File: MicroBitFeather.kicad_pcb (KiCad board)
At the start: 2 copper layers, 67.3 x 35.6 mm, 16 parts, among them J1 Feather_Long, J2 Barrel_Jack_MountingPin, J3 Feather_Short, J4 NeoPixels, J5 microbit_edge_connector, U1 74AHCT125, U2 MCP1702-3302E_TO92

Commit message: 5V wiring.
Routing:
- net +5V: track 0.00 -> 53.0 mm
- added copper zone on F.Cu, net +5V
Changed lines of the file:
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@@
     (thickness 1.6)
     (drawings 12)
-    (tracks 0)
+    (tracks 16)
     (zones 0)
     (modules 16)
@@
   )
   (setup
-    (last_trace_width 0.25)
+    (last_trace_width 0.508)
+    (user_trace_width 0.508)
+    (user_trace_width 1.016)
     (trace_clearance 0.2)
-    (zone_clearance 0.508)
+    (zone_clearance 0.3048)
     (zone_45_only no)
     (trace_min 0.2)
@@
     (pad_to_mask_clearance 0)
     (aux_axis_origin 0 0)
-    (visible_elements FFFEF77F)
+    (visible_elements FFFEE77F)
     (pcbplotparams
       (layerselection 0x00030_80000001)
@@
   (gr_arc (start 119.38 118.11) (end 119.38 119.38) (angle 90) (layer Edge.Cuts) (width 0.15))
   (gr_arc (start 119.38 85.09) (end 118.11 85.09) (angle 90) (layer Edge.Cuts) (width 0.15))
+  (segment (start 157.48 101.6) (end 154.94 104.14) (width 0.508) (layer F.Cu) (net 1))
+  (segment (start 154.94 104.14) (end 154.94 106.68) (width 0.508) (layer F.Cu) (net 1))
+  (segment (start 133.35 100.33) (end 129.54 96.52) (width 0.508) (layer F.Cu) (net 1))
+  (segment (start 135.89 96.52) (end 135.89 97.79) (width 0.508) (layer F.Cu) (net 1))
+  (segment (start 135.89 97.79) (end 133.35 100.33) (width 0.508) (layer F.Cu) (net 1))
+  (segment (start 140.97 96.52) (end 139.411999 98.078001) (width 1.016) (layer F.Cu) (net 1))
+  (segment (start 139.411999 98.078001) (end 137.448001 98.078001) (width 1.016) (layer F.Cu) (net 1))
+  (segment (start 137.448001 98.078001) (end 135.89 96.52) (width 1.016) (layer F.Cu) (net 1))
+  (segment (start 157.48 101.6) (end 154.94 99.06) (width 1.016) (layer F.Cu) (net 1))
+  (segment (start 154.94 99.06) (end 143.51 99.06) (width 1.016) (layer F.Cu) (net 1))
+  (segment (start 141.819999 97.369999) (end 140.97 96.52) (width 1.016) (layer F.Cu) (net 1))
+  (segment (start 143.51 99.06) (end 141.819999 97.369999) (width 1.016) (layer F.Cu) (net 1))
+  (segment (start 167.005 106.68) (end 164.989 106.68) (width 1.016) (layer F.Cu) (net 1))
+  (segment (start 164.989 106.68) (end 159.909 101.6) (width 1.016) (layer F.Cu) (net 1))
+  (segment (start 159.909 101.6) (end 158.61137 101.6) (width 1.016) (layer F.Cu) (net 1))
+  (segment (start 158.61137 101.6) (end 157.48 101.6) (width 1.016) (layer F.Cu) (net 1))
+  (zone (net 1) (net_name +5V) (layer F.Cu) (hatch edge 0.508)
+    (connect_pads (clearance 0.3048))
+    (min_thickness 0.254)
+    (fill (arc_segments 16) (thermal_gap 0.508) (thermal_bridge_width 0.508))
+    (polygon
+      (pts
+        (xy 180.34 114.3) (xy 166.37 114.3) (xy 166.37 100.33) (xy 180.34 100.33)
+      )
+    )
+  )
 )

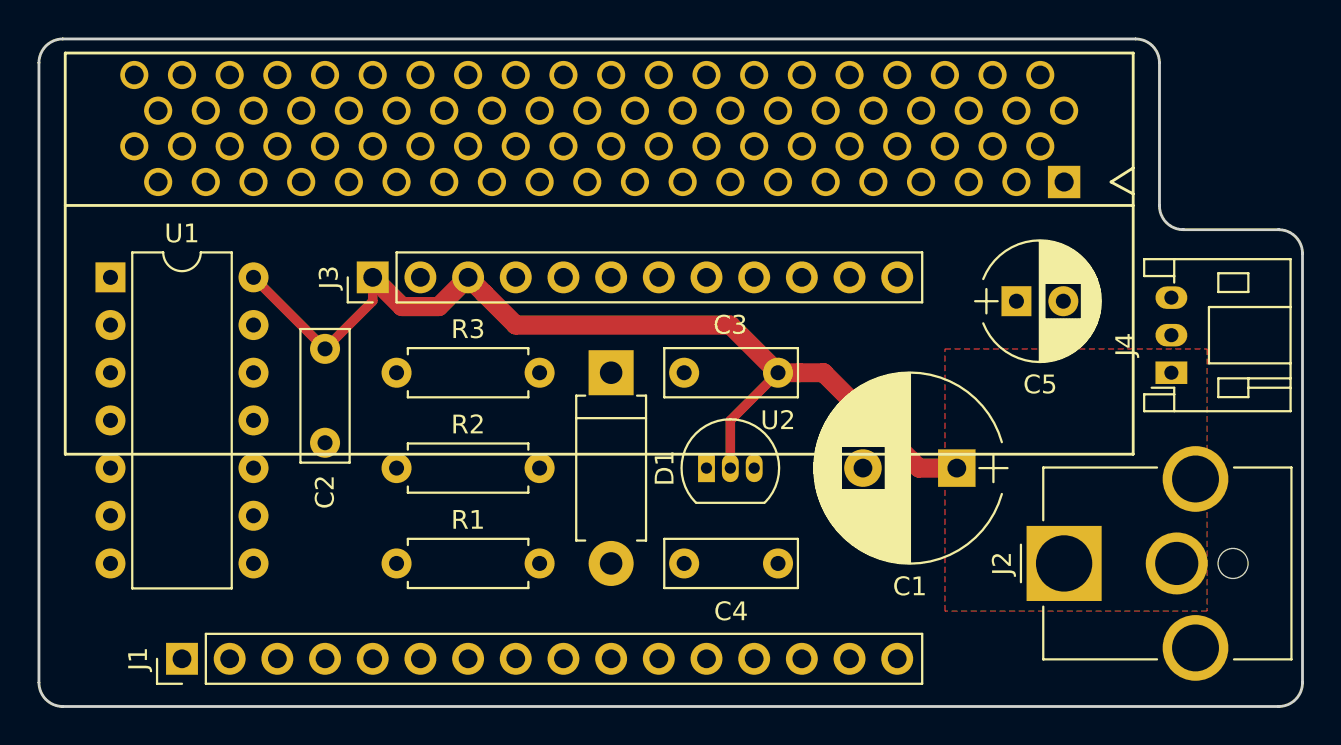
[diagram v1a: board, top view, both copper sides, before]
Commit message: 3V3 wiring.
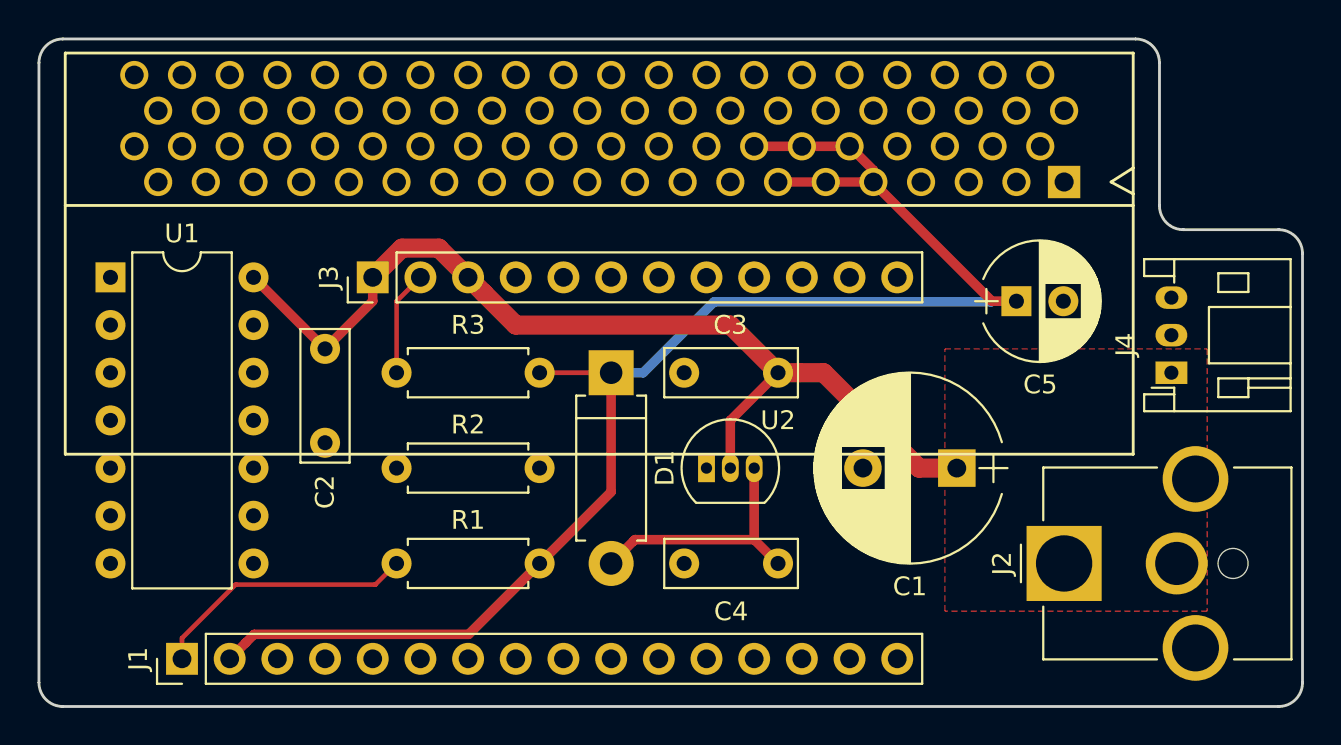
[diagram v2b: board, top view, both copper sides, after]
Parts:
- moved R3 7.62 mm to (144.8, 101.6), turned to 180 degrees
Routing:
- net +3V3: track 0.00 -> 80.2 mm
- net Net-(J1-Pad1): track 0.00 -> 14.2 mm
- net Net-(C4-Pad1): track 0.00 -> 13.8 mm
- net Net-(J3-Pad2): track 0.00 -> 5.61 mm
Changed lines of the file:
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@@
   (general
     (links 79)
-    (no_connects 79)
+    (no_connects 71)
     (area 115.424999 71.584999 217.260002 148.48)
     (thickness 1.6)
     (drawings 12)
-    (tracks 16)
+    (tracks 48)
     (zones 0)
     (modules 16)
@@
   )
   (module Resistors_THT:R_Axial_DIN0207_L6.3mm_D2.5mm_P7.62mm_Horizontal (layer F.Cu)
-    (at 137.16 101.6)
+    (at 144.78 101.6 180)
     (descr "Resistor, Axial_DIN0207 series, Axial, Horizontal, pin pitch=7.62mm, 0.25W = 1/4W, length*diameter=6.3*2.5mm^2, http://cdn-reichelt.de/documents/datenblatt/B400/1_4W%23YAG.pdf")
     (tags "Resistor Axial_DIN0207 series Axial Horizontal pin pitch 7.62mm 0.25W = 1/4W length 6.3mm diameter 2.5mm")
-    (fp_text reference R3 (at 3.81 -2.31) (layer F.SilkS)
-      (effects (font (size 1 1) (thickness 0.15)))
-    )
-    (fp_text value 10K (at 3.81 2.31) (layer F.Fab)
+    (fp_text reference R3 (at 3.81 2.54 180) (layer F.SilkS)
+      (effects (font (size 1 1) (thickness 0.15)))
+    )
+    (fp_text value 10K (at 3.81 2.31 180) (layer F.Fab)
       (effects (font (size 1 1) (thickness 0.15)))
     )
@@
     (fp_line (start 8.7 1.6) (end 8.7 -1.6) (layer F.CrtYd) (width 0.05))
     (fp_line (start 8.7 -1.6) (end -1.05 -1.6) (layer F.CrtYd) (width 0.05))
-    (pad 1 thru_hole circle (at 0 0) (size 1.6 1.6) (drill 0.8) (layers *.Cu *.Mask)
+    (pad 1 thru_hole circle (at 0 0 180) (size 1.6 1.6) (drill 0.8) (layers *.Cu *.Mask)
       (net 4 +3V3))
-    (pad 2 thru_hole oval (at 7.62 0) (size 1.6 1.6) (drill 0.8) (layers *.Cu *.Mask)
+    (pad 2 thru_hole oval (at 7.62 0 180) (size 1.6 1.6) (drill 0.8) (layers *.Cu *.Mask)
       (net 19 "Net-(J3-Pad2)"))
     (model ${KISYS3DMOD}/Resistors_THT.3dshapes/R_Axial_DIN0207_L6.3mm_D2.5mm_P7.62mm_Horizontal.wrl
@@
   (gr_arc (start 119.38 118.11) (end 119.38 119.38) (angle 90) (layer Edge.Cuts) (width 0.15))
   (gr_arc (start 119.38 85.09) (end 118.11 85.09) (angle 90) (layer Edge.Cuts) (width 0.15))
+  (segment (start 140.97 96.52) (end 139.411999 94.961999) (width 1.016) (layer F.Cu) (net 1))
+  (segment (start 139.411999 94.961999) (end 137.448001 94.961999) (width 1.016) (layer F.Cu) (net 1))
+  (segment (start 137.448001 94.961999) (end 135.89 96.52) (width 1.016) (layer F.Cu) (net 1))
   (segment (start 157.48 101.6) (end 154.94 104.14) (width 0.508) (layer F.Cu) (net 1))
   (segment (start 154.94 104.14) (end 154.94 106.68) (width 0.508) (layer F.Cu) (net 1))
@@
   (segment (start 135.89 96.52) (end 135.89 97.79) (width 0.508) (layer F.Cu) (net 1))
   (segment (start 135.89 97.79) (end 133.35 100.33) (width 0.508) (layer F.Cu) (net 1))
-  (segment (start 140.97 96.52) (end 139.411999 98.078001) (width 1.016) (layer F.Cu) (net 1))
-  (segment (start 139.411999 98.078001) (end 137.448001 98.078001) (width 1.016) (layer F.Cu) (net 1))
-  (segment (start 137.448001 98.078001) (end 135.89 96.52) (width 1.016) (layer F.Cu) (net 1))
   (segment (start 157.48 101.6) (end 154.94 99.06) (width 1.016) (layer F.Cu) (net 1))
   (segment (start 154.94 99.06) (end 143.51 99.06) (width 1.016) (layer F.Cu) (net 1))
@@
   (segment (start 159.909 101.6) (end 158.61137 101.6) (width 1.016) (layer F.Cu) (net 1))
   (segment (start 158.61137 101.6) (end 157.48 101.6) (width 1.016) (layer F.Cu) (net 1))
+  (segment (start 156.21 110.49) (end 149.86 110.49) (width 0.508) (layer F.Cu) (net 3))
+  (segment (start 149.86 110.49) (end 149.789999 110.560001) (width 0.508) (layer F.Cu) (net 3))
+  (segment (start 149.789999 110.560001) (end 148.59 111.76) (width 0.508) (layer F.Cu) (net 3))
+  (segment (start 156.21 106.68) (end 156.21 110.49) (width 0.508) (layer F.Cu) (net 3))
+  (segment (start 156.21 110.49) (end 157.48 111.76) (width 0.508) (layer F.Cu) (net 3))
+  (segment (start 158.75 89.54) (end 156.21 89.54) (width 0.508) (layer F.Cu) (net 4))
+  (segment (start 161.29 89.54) (end 158.75 89.54) (width 0.508) (layer F.Cu) (net 4))
+  (segment (start 162.56 91.44) (end 162.56 90.81) (width 0.508) (layer F.Cu) (net 4))
+  (segment (start 162.56 90.81) (end 161.29 89.54) (width 0.508) (layer F.Cu) (net 4))
+  (segment (start 160.02 91.44) (end 157.48 91.44) (width 0.508) (layer F.Cu) (net 4))
+  (segment (start 162.56 91.44) (end 160.02 91.44) (width 0.508) (layer F.Cu) (net 4))
+  (segment (start 170.18 97.79) (end 168.872 97.79) (width 0.508) (layer F.Cu) (net 4))
+  (segment (start 168.872 97.79) (end 162.56 91.478) (width 0.508) (layer F.Cu) (net 4))
+  (segment (start 162.56 91.478) (end 162.56 91.44) (width 0.508) (layer F.Cu) (net 4))
+  (segment (start 144.78 111.76) (end 141.004001 115.535999) (width 0.508) (layer F.Cu) (net 4))
+  (segment (start 141.004001 115.535999) (end 129.574001 115.535999) (width 0.508) (layer F.Cu) (net 4))
+  (segment (start 129.574001 115.535999) (end 129.119999 115.990001) (width 0.508) (layer F.Cu) (net 4))
+  (segment (start 129.119999 115.990001) (end 128.27 116.84) (width 0.508) (layer F.Cu) (net 4))
+  (segment (start 148.59 101.6) (end 148.59 107.95) (width 0.508) (layer F.Cu) (net 4))
+  (segment (start 148.59 107.95) (end 144.78 111.76) (width 0.508) (layer F.Cu) (net 4))
+  (segment (start 148.59 101.6) (end 144.78 101.6) (width 0.25) (layer F.Cu) (net 4))
+  (segment (start 148.59 101.6) (end 150.298 101.6) (width 0.508) (layer B.Cu) (net 4))
+  (segment (start 150.298 101.6) (end 154.073999 97.824001) (width 0.508) (layer B.Cu) (net 4))
+  (segment (start 154.073999 97.824001) (end 168.837999 97.824001) (width 0.508) (layer B.Cu) (net 4))
+  (segment (start 168.837999 97.824001) (end 168.872 97.79) (width 0.508) (layer B.Cu) (net 4))
+  (segment (start 168.872 97.79) (end 170.18 97.79) (width 0.508) (layer B.Cu) (net 4))
+  (segment (start 137.16 111.76) (end 136.034999 112.885001) (width 0.25) (layer F.Cu) (net 5))
+  (segment (start 136.034999 112.885001) (end 128.584999 112.885001) (width 0.25) (layer F.Cu) (net 5))
+  (segment (start 128.584999 112.885001) (end 125.73 115.74) (width 0.25) (layer F.Cu) (net 5))
+  (segment (start 125.73 115.74) (end 125.73 116.84) (width 0.25) (layer F.Cu) (net 5))
+  (segment (start 137.16 101.6) (end 137.16 97.79) (width 0.25) (layer F.Cu) (net 19))
+  (segment (start 137.16 97.79) (end 138.43 96.52) (width 0.25) (layer F.Cu) (net 19))
   (zone (net 1) (net_name +5V) (layer F.Cu) (hatch edge 0.508)
     (connect_pads (clearance 0.3048))
